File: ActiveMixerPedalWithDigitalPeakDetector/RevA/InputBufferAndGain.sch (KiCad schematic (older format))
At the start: 7 parts, among them U2 TL072

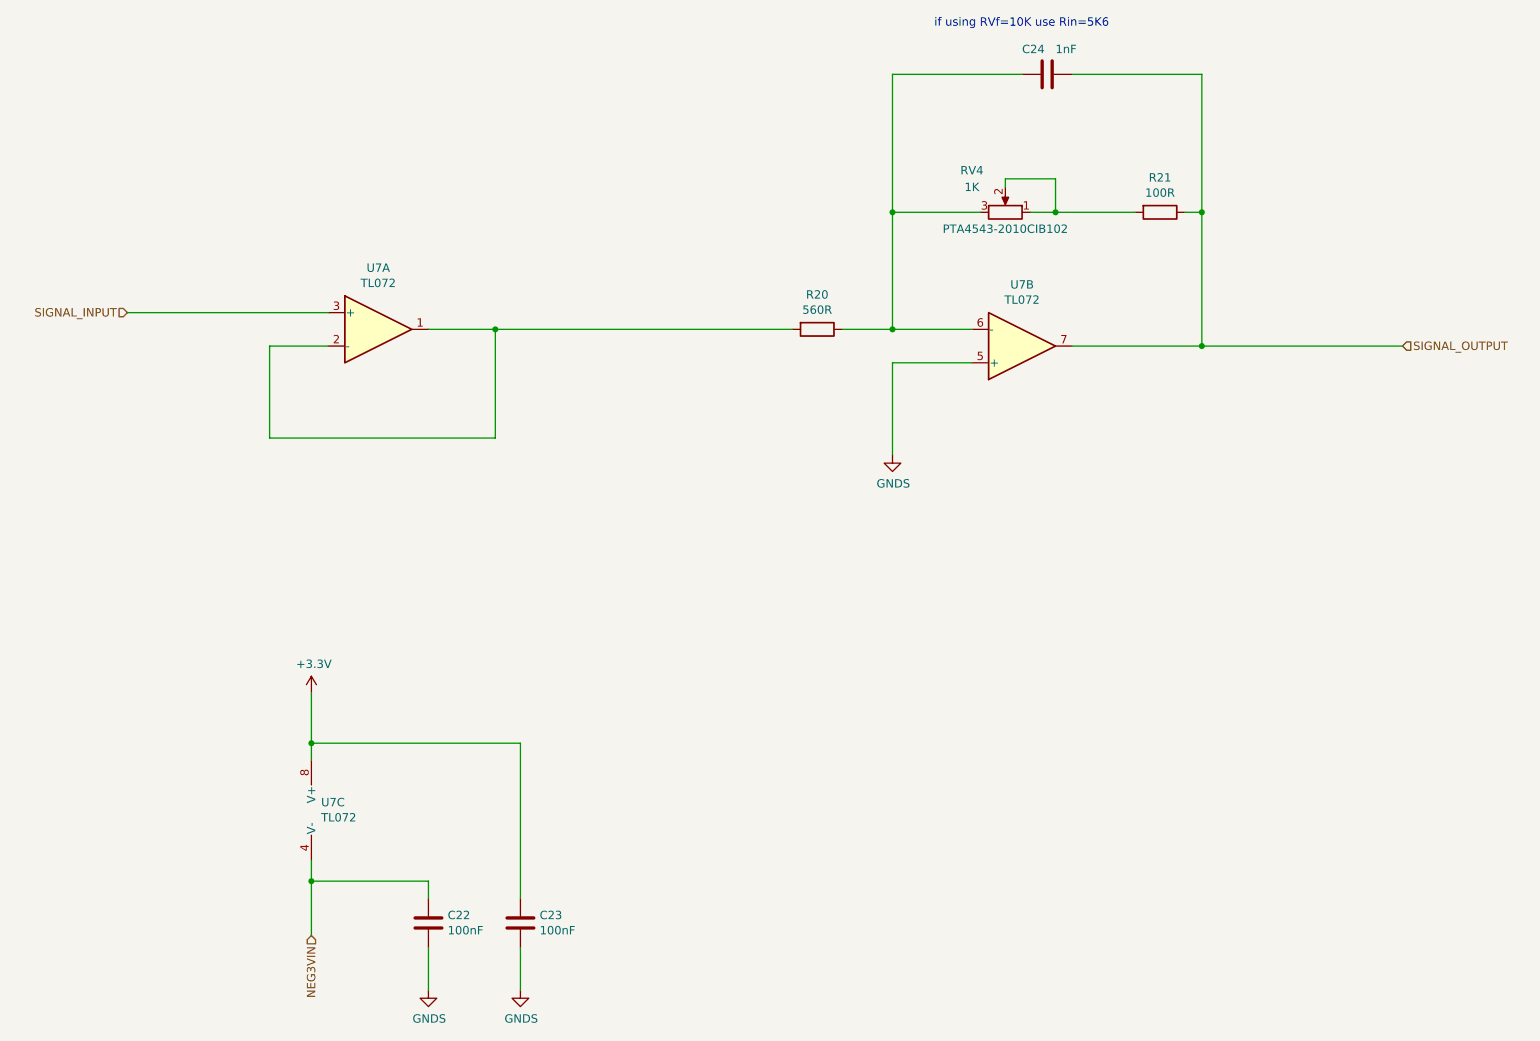
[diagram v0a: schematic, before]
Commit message: schematic update
updated resistor (Rin) to 1K/10K
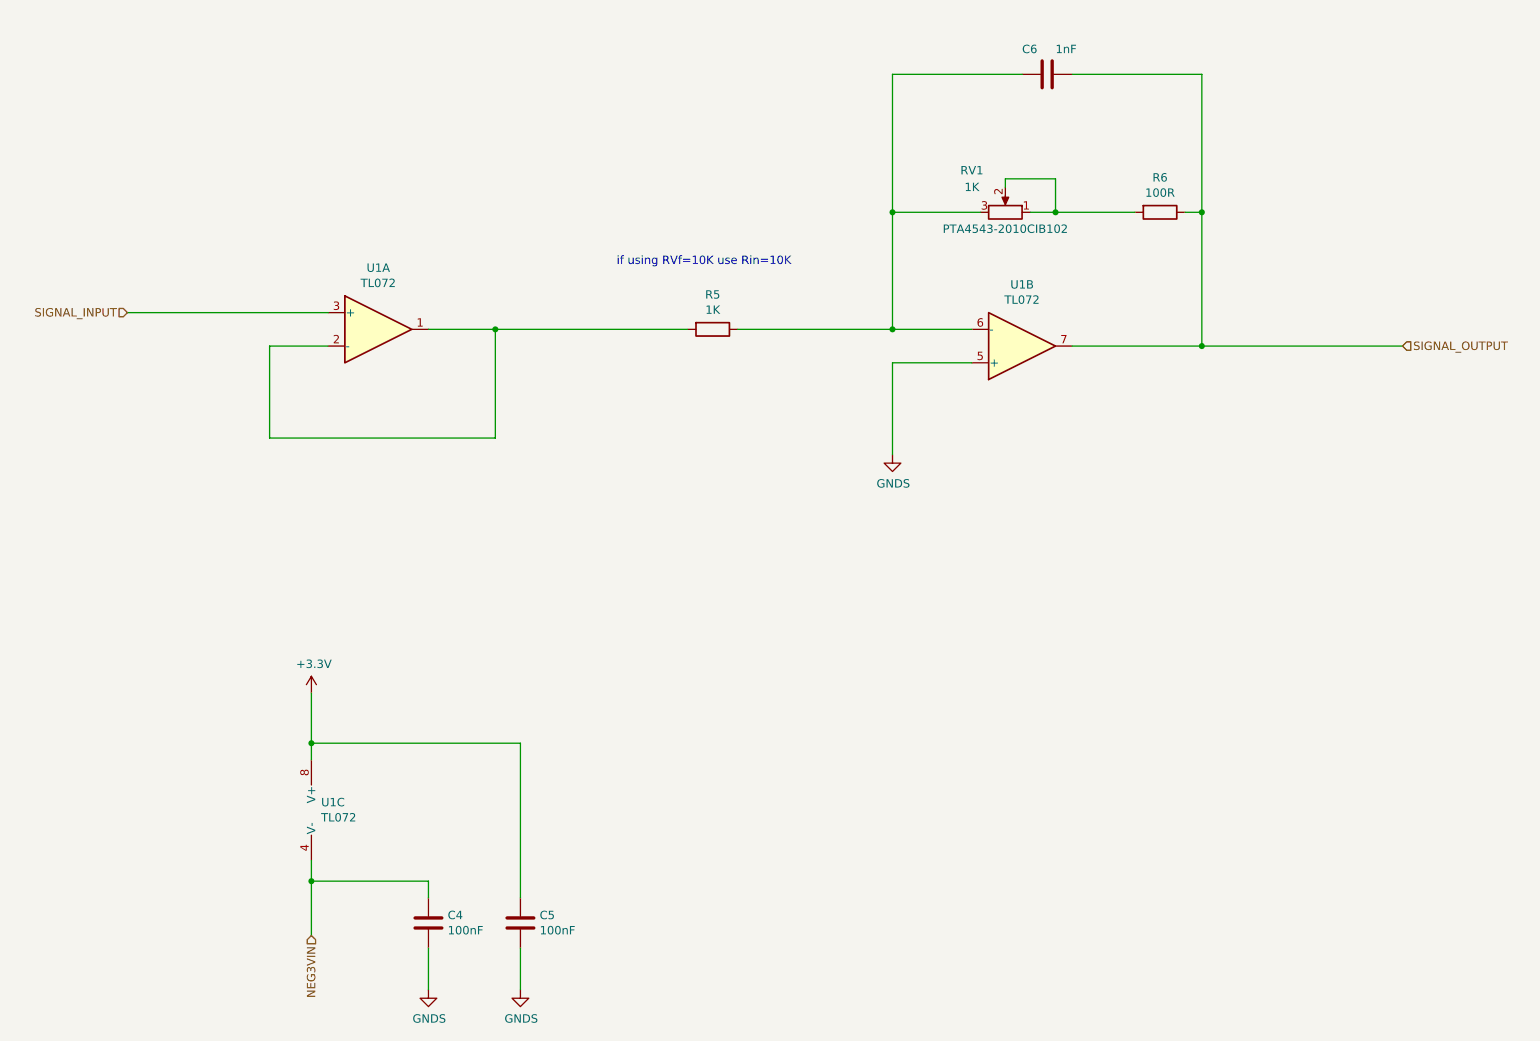
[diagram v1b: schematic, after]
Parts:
- R5: value 560R -> 1K
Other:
- note added: "if using RVf=10K use Rin=10K\n"
- note removed: "if using RVf=10K use Rin=5K6"
- moved on the sheet: R5
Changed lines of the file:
@@
 L Device:R R?
 U 1 1 5F59292E
-P 6225 2875
+P 5600 2875
 AR Path="/5F3F1F31/5F59292E" Ref="R?"  Part="1"
 AR Path="/5F512144/5F59292E" Ref="R?"  Part="1"
@@
 AR Path="/5F5BB12C/5F59292E" Ref="R15"  Part="1"
 AR Path="/5F5BCC25/5F59292E" Ref="R20"  Part="1"
-F 0 "R20" V 6018 2875 50  0000 C CNN
-F 1 "560R" V 6109 2875 50  0000 C CNN
-F 2 "Resistor_SMD:R_0805_2012Metric_Pad1.15x1.40mm_HandSolder" V 6155 2875 50  0001 C CNN
-F 3 "~" H 6225 2875 50  0001 C CNN
-	1    6225 2875
+F 0 "R5" V 5393 2875 50  0000 C CNN
+F 1 "1K" V 5484 2875 50  0000 C CNN
+F 2 "Resistor_SMD:R_0805_2012Metric_Pad1.15x1.40mm_HandSolder" V 5530 2875 50  0001 C CNN
+F 3 "~" H 5600 2875 50  0001 C CNN
+	1    5600 2875
 	0    1    1    0
 $EndComp
@@
 AR Path="/5F5BB12C/5F59293F" Ref="RV3"  Part="1"
 AR Path="/5F5BCC25/5F59293F" Ref="RV4"  Part="1"
-F 0 "RV4" V 7600 1975 50  0000 C CNN
+F 0 "RV1" V 7600 1975 50  0000 C CNN
 F 1 "1K" V 7500 1975 50  0000 C CNN
 F 2 "Bourn_PTA_Slider:Slider_PTA4543_60MM" H 7350 2175 50  0001 C CNN
@@
 Connection ~ 6675 2875
 Wire Wire Line
-	6675 2875 6375 2875
+	6675 2875 5750 2875
 Wire Wire Line
 	8525 2975 9725 2975
-Text Notes 6925 1075 0    50   ~ 0
-if using RVf=10K use Rin=5K6
+Text Notes 5025 2500 0    50   ~ 0
+if using RVf=10K use Rin=10K\n
 Connection ~ 8525 2975
 Wire Wire Line
@@
 AR Path="/5F5BB12C/5F592956" Ref="R16"  Part="1"
 AR Path="/5F5BCC25/5F592956" Ref="R21"  Part="1"
-F 0 "R21" V 8068 2175 50  0000 C CNN
+F 0 "R6" V 8068 2175 50  0000 C CNN
 F 1 "100R" V 8159 2175 50  0000 C CNN
 F 2 "Resistor_SMD:R_0805_2012Metric_Pad1.15x1.40mm_HandSolder" V 8205 2175 50  0001 C CNN
@@
 AR Path="/5F5BB12C/5F59295D" Ref="C18"  Part="1"
 AR Path="/5F5BCC25/5F59295D" Ref="C24"  Part="1"
-F 0 "C24" V 7450 1200 50  0000 L CNN
+F 0 "C6" V 7450 1200 50  0000 L CNN
 F 1 "1nF" V 7450 1400 50  0000 L CNN
 F 2 "Capacitor_SMD:C_0805_2012Metric_Pad1.15x1.40mm_HandSolder" H 7638 1200 50  0001 C CNN
@@
 Connection ~ 8525 2175
 Wire Wire Line
-	4300 2875 6075 2875
+	4300 2875 5450 2875
 $Comp
 L Amplifier_Operational:TL072 U2
@@
 AR Path="/5F5BB12C/5F59AE7C" Ref="U5"  Part="1"
 AR Path="/5F5BCC25/5F59AE7C" Ref="U7"  Part="1"
-F 0 "U7" H 3600 3242 50  0000 C CNN
+F 0 "U1" H 3600 3242 50  0000 C CNN
 F 1 "TL072" H 3600 3151 50  0000 C CNN
 F 2 "Package_SO:SOIC-8_3.9x4.9mm_P1.27mm" H 3600 2875 50  0001 C CNN
@@
 AR Path="/5F5BB12C/5F59C9C2" Ref="U5"  Part="2"
 AR Path="/5F5BCC25/5F59C9C2" Ref="U7"  Part="2"
-F 0 "U7" H 7450 2608 50  0000 C CNN
+F 0 "U1" H 7450 2608 50  0000 C CNN
 F 1 "TL072" H 7450 2699 50  0000 C CNN
 F 2 "Package_SO:SOIC-8_3.9x4.9mm_P1.27mm" H 7450 2975 50  0001 C CNN
@@
 AR Path="/5F5BB12C/5F59E5A5" Ref="U5"  Part="3"
 AR Path="/5F5BCC25/5F59E5A5" Ref="U7"  Part="3"
-F 0 "U7" H 3258 5796 50  0000 L CNN
+F 0 "U1" H 3258 5796 50  0000 L CNN
 F 1 "TL072" H 3258 5705 50  0000 L CNN
 F 2 "Package_SO:SOIC-8_3.9x4.9mm_P1.27mm" H 3300 5750 50  0001 C CNN
@@
 AR Path="/5F5BB12C/5F5D3555" Ref="C16"  Part="1"
 AR Path="/5F5BCC25/5F5D3555" Ref="C22"  Part="1"
-F 0 "C22" H 4015 6471 50  0000 L CNN
+F 0 "C4" H 4015 6471 50  0000 L CNN
 F 1 "100nF" H 4015 6380 50  0000 L CNN
 F 2 "Capacitor_SMD:C_0805_2012Metric_Pad1.15x1.40mm_HandSolder" H 3938 6275 50  0001 C CNN
@@
 AR Path="/5F5BB12C/5F5D446F" Ref="C17"  Part="1"
 AR Path="/5F5BCC25/5F5D446F" Ref="C23"  Part="1"
-F 0 "C23" H 4565 6471 50  0000 L CNN
+F 0 "C5" H 4565 6471 50  0000 L CNN
 F 1 "100nF" H 4565 6380 50  0000 L CNN
 F 2 "Capacitor_SMD:C_0805_2012Metric_Pad1.15x1.40mm_HandSolder" H 4488 6275 50  0001 C CNN
@@
 AR Path="/5F5BB12C/5F596316" Ref="#PWR0135"  Part="1"
 AR Path="/5F5BCC25/5F596316" Ref="#PWR0147"  Part="1"
-F 0 "#PWR0147" H 3200 4900 50  0001 C CNN
+F 0 "#PWR0111" H 3200 4900 50  0001 C CNN
 F 1 "+3.3V" H 3215 5223 50  0000 C CNN
 F 2 "" H 3200 5050 50  0001 C CNN
@@
 AR Path="/5F5B9EED/5F6D4091" Ref="#PWR020"  Part="1"
 AR Path="/5F5BB12C/5F6D4091" Ref="#PWR023"  Part="1"
-F 0 "#PWR026" H 6675 3375 50  0001 C CNN
+F 0 "#PWR017" H 6675 3375 50  0001 C CNN
 F 1 "GNDS" H 6680 3452 50  0000 C CNN
 F 2 "" H 6675 3625 50  0001 C CNN
@@
 AR Path="/5F5B9EED/5F6D63E7" Ref="#PWR018"  Part="1"
 AR Path="/5F5BB12C/5F6D63E7" Ref="#PWR021"  Part="1"
-F 0 "#PWR024" H 3900 6575 50  0001 C CNN
+F 0 "#PWR015" H 3900 6575 50  0001 C CNN
 F 1 "GNDS" H 3905 6652 50  0000 C CNN
 F 2 "" H 3900 6825 50  0001 C CNN
@@
 AR Path="/5F5B9EED/5F6D6B89" Ref="#PWR019"  Part="1"
 AR Path="/5F5BB12C/5F6D6B89" Ref="#PWR022"  Part="1"
-F 0 "#PWR025" H 4450 6575 50  0001 C CNN
+F 0 "#PWR016" H 4450 6575 50  0001 C CNN
 F 1 "GNDS" H 4455 6652 50  0000 C CNN
 F 2 "" H 4450 6825 50  0001 C CNN
